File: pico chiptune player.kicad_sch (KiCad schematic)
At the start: 24 parts, among them J1 MicroSD, J2 Speaker Out, SW1 Play / Pause, SW2 Next, SW3 Previous, U1 AY-3-8910, U2 PAM8302AAS, U3 0.96"OLED_I2C

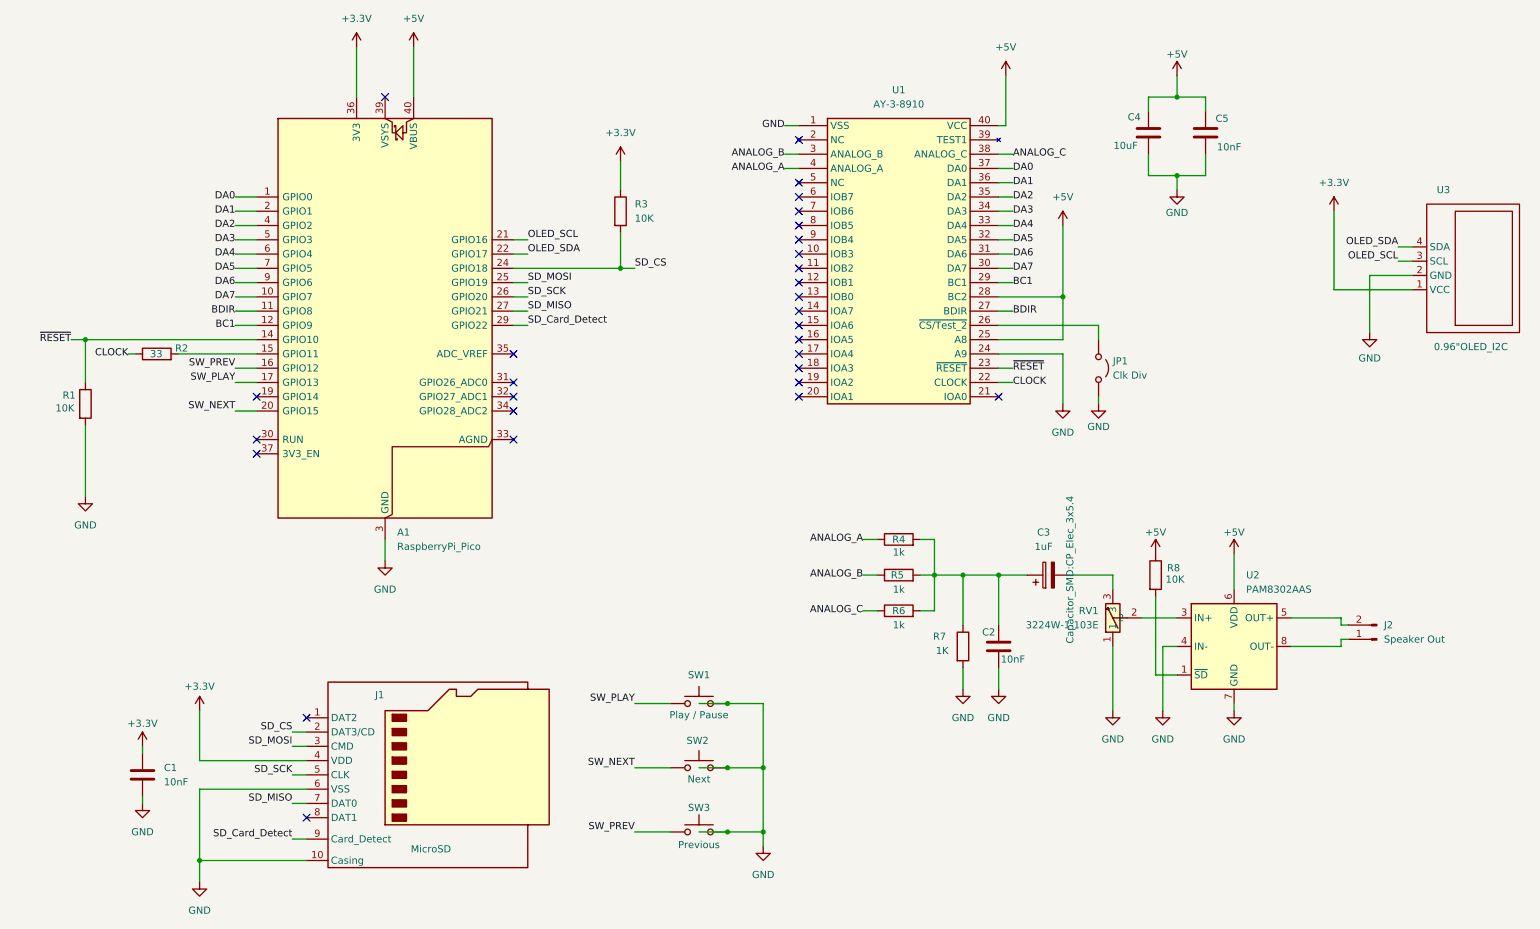
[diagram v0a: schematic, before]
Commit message: docs, sch: rev 0.2 — align HARDWARE.md with schematic (SSOT)
Schematic is the single source of truth; HARDWARE.md updated to match:
- +5V rail sourced from Pico Pin 40 (VBUS), not Pin 39 (VSYS)
- Document R8 pull-up on PAM8302 ~SD; correct R3 as SD_CS pull-up
- PAM8302 pinout re-mapped to KiCad Amplifier_Audio:PAM8302AAS symbol
- Capacitor types (C3 polarized electrolytic, C4 MLCC ceramic)
  reflect actual schematic footprints
- Added Revision History section

Schematic-side changes (by Terence): no_connect markers on unused Pico
and AY-3-8910 pins, C1 footprint set. Title-block rev bumped 0.1 -> 0.2
in .kicad_sch and .kicad_pcb; date to 2026-08-12.

Co-Authored-By: Claude Opus 4.7 <noreply@anthropic.com>
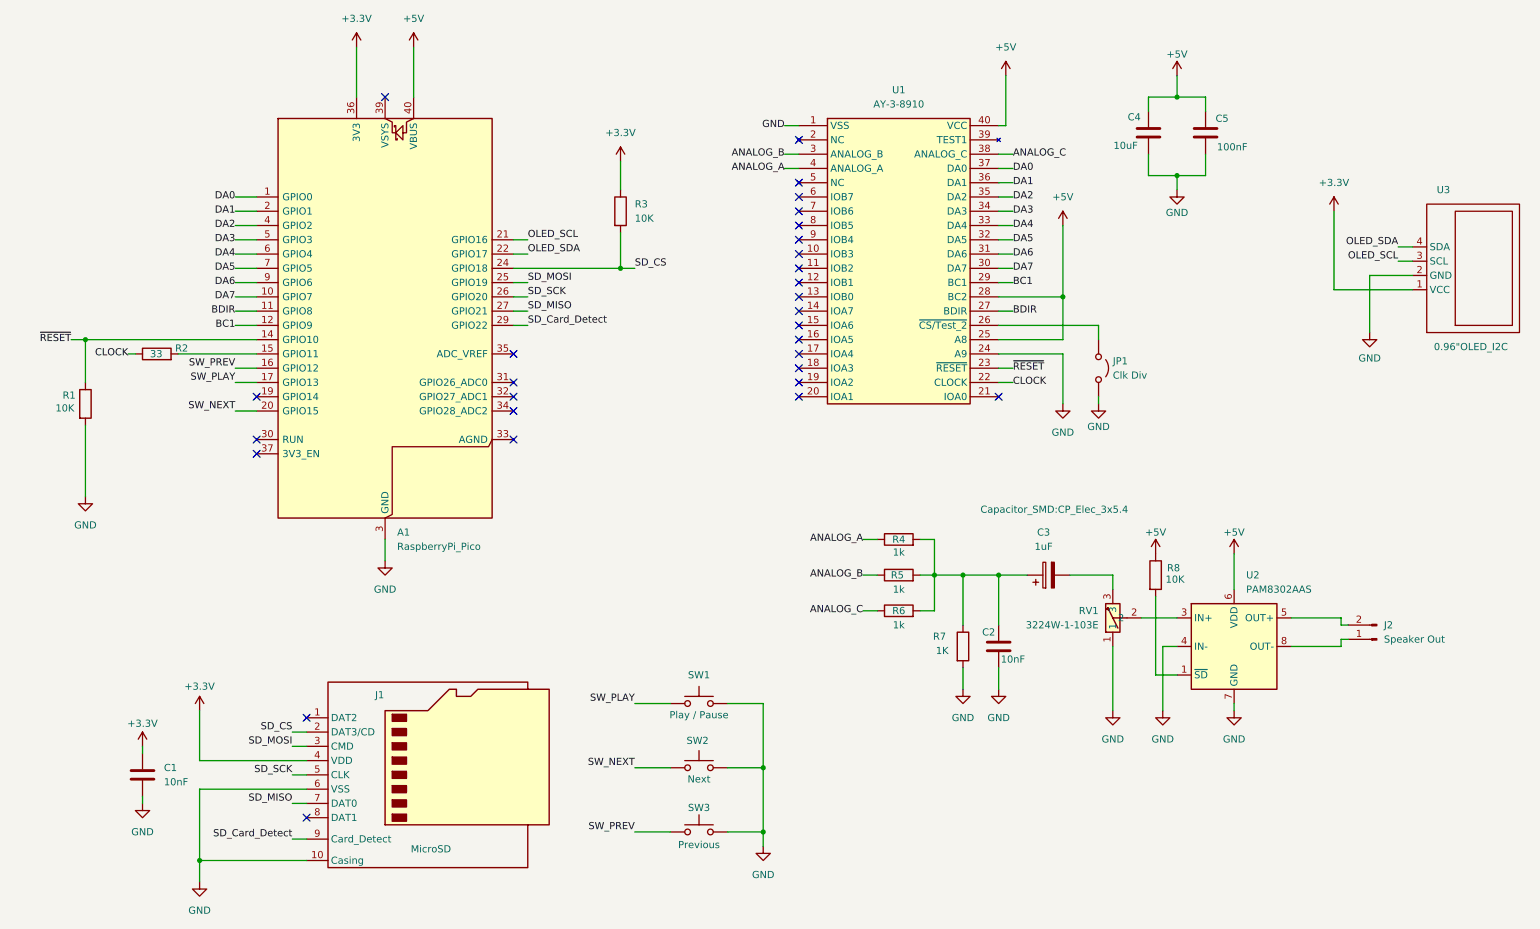
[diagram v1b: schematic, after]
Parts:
- C1: footprint (none) -> Capacitor_SMD:C_0805_2012Metric_Pad1.18x1.45mm_HandSolder
- C4: footprint Capacitor_SMD:C_0805_2012Metric_Pad1.18x1.45mm_HandSolder -> Capacitor_SMD:CP_Elec_3x5.3
- C5: value 10nF -> 100nF
- U2: footprint Package_SO:SOIC-8_5.3x5.3mm_P1.27mm -> Package_SO:SOIC-8_3.9x4.9mm_P1.27mm
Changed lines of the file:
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@@
 	(title_block
 		(title "Pico Chiptune Player")
-		(date "2026-08-08")
-		(rev "0.1")
+		(date "2026-08-12")
+		(rev "0.2")
 		(company "MotionFxDesign")
 		(comment 1 "Terence Ang / MotionFxDesign")
@@
 	)
 	(junction
-		(at 137.16 139.7)
-		(diameter 0)
-		(color 0 0 0 0)
-	)
-	(junction
 		(at 217.17 45.72)
 		(diameter 0)
@@
 	)
 	(junction
-		(at 137.16 162.56)
-		(diameter 0)
-		(color 0 0 0 0)
-	)
-	(junction
 		(at 22.86 74.93)
 		(diameter 0)
@@
 	)
 	(junction
-		(at 137.16 151.13)
-		(diameter 0)
-		(color 0 0 0 0)
-	)
-	(junction
 		(at 173.99 116.84)
 		(diameter 0)
@@
 	)
 	(no_connect
-		(at 53.34 85.09)
-	)
-	(no_connect
 		(at 149.86 74.93)
 	)
@@
 	)
 	(no_connect
+		(at 53.34 85.09)
+	)
+	(no_connect
 		(at 149.86 64.77)
 	)
@@
 	(wire
 		(pts
-			(xy 132.08 151.13) (xy 137.16 151.13)
-		)
-		(stroke
-			(width 0)
-			(type default)
-		)
-	)
-	(wire
-		(pts
 			(xy 22.86 74.93) (xy 22.86 82.55)
 		)
@@
 	(wire
 		(pts
-			(xy 132.08 139.7) (xy 137.16 139.7)
-		)
-		(stroke
-			(width 0)
-			(type default)
-		)
-	)
-	(wire
-		(pts
 			(xy 217.17 31.75) (xy 222.25 31.75)
 		)
@@
 	(wire
 		(pts
-			(xy 132.08 162.56) (xy 137.16 162.56)
-		)
-		(stroke
-			(width 0)
-			(type default)
-		)
-	)
-	(wire
-		(pts
 			(xy 22.86 90.17) (xy 22.86 102.87)
 		)
@@
 		(in_pos_files yes)
 		(dnp no)
-		(fields_autoplaced yes)
 		(property "Reference" "C3"
 			(at 193.421 109.22 90)
@@
 		)
 		(property "Footprint" "Capacitor_SMD:CP_Elec_3x5.4"
-			(at 198.12 115.8748 0)
+			(at 195.326 105.156 90)
 			(show_name no)
 			(do_not_autoplace no)
@@
 			)
 		)
-		(property "Value" "10nF"
+		(property "Value" "100nF"
 			(at 224.282 40.64 0)
 			(show_name no)
@@
 			)
 		)
-		(property "Footprint" "Capacitor_SMD:C_0805_2012Metric_Pad1.18x1.45mm_HandSolder"
+		(property "Footprint" "Capacitor_SMD:CP_Elec_3x5.3"
 			(at 212.09 38.1 0)
 			(hide yes)
@@
 			)
 		)
-		(property "Footprint" ""
+		(property "Footprint" "Capacitor_SMD:C_0805_2012Metric_Pad1.18x1.45mm_HandSolder"
 			(at 33.9852 156.21 0)
 			(hide yes)
@@
 			)
 		)
-		(property "Footprint" "Package_SO:SOIC-8_5.3x5.3mm_P1.27mm"
+		(property "Footprint" "Package_SO:SOIC-8_3.9x4.9mm_P1.27mm"
 			(at 227.33 129.54 0)
 			(hide yes)
